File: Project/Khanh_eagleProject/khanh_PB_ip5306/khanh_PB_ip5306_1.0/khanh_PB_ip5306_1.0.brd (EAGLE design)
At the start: 27 x 16 mm, 18 parts

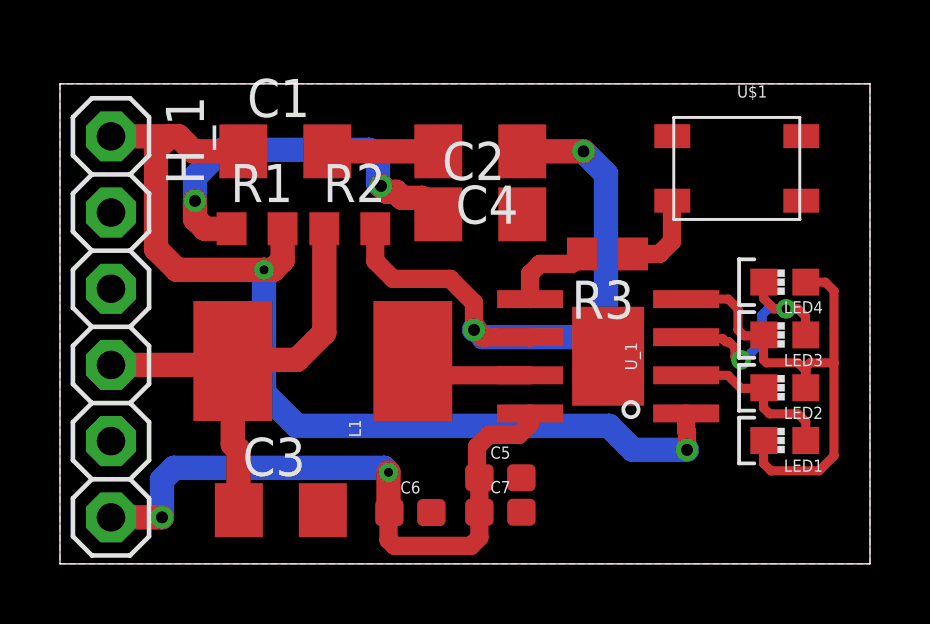
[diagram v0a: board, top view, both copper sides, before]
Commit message: chỉnh sửa pcd mạch sạc ip5306
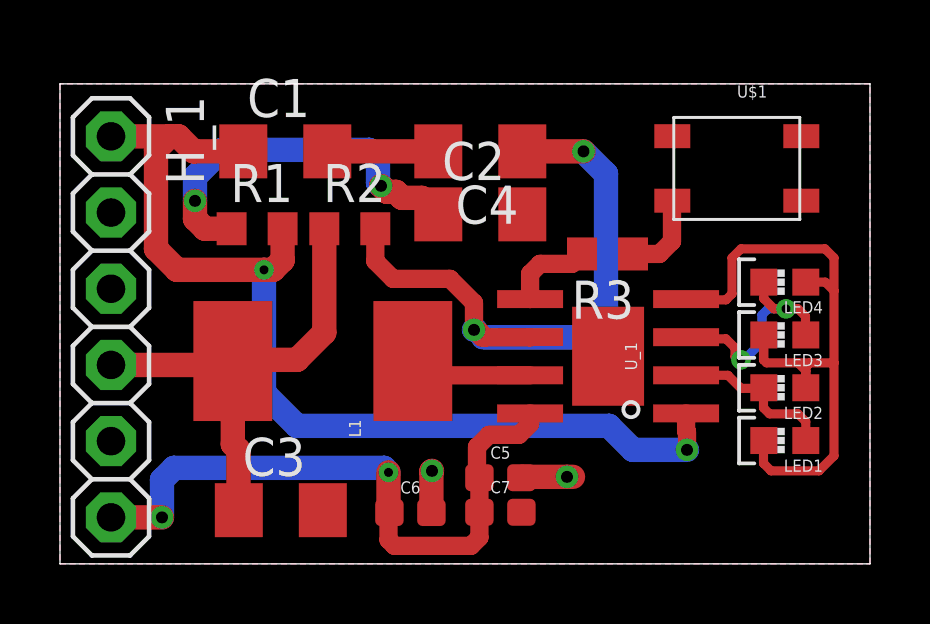
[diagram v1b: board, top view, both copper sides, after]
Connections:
- net VIN renamed S'HO
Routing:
- net N$7: track 18.2 -> 23.4 mm
- net GND: track 3.70 -> 6.83 mm, vias 0 -> 2
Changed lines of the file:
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@@
 <grid distance="0.1" unitdist="mm" unit="mm" style="lines" multiple="1" display="yes" altdistance="0.05" altunitdist="mm" altunit="mm"/>
 <layers>
-<layer number="1" name="Top" color="4" fill="1" visible="no" active="yes"/>
+<layer number="1" name="Top" color="4" fill="1" visible="yes" active="yes"/>
 <layer number="2" name="Route2" color="1" fill="3" visible="no" active="no"/>
 <layer number="3" name="Route3" color="4" fill="3" visible="no" active="no"/>
@@
 <layer number="21" name="tPlace" color="7" fill="1" visible="no" active="yes"/>
 <layer number="22" name="bPlace" color="7" fill="1" visible="no" active="yes"/>
-<layer number="23" name="tOrigins" color="15" fill="1" visible="no" active="yes"/>
+<layer number="23" name="tOrigins" color="15" fill="1" visible="yes" active="yes"/>
 <layer number="24" name="bOrigins" color="15" fill="1" visible="yes" active="yes"/>
 <layer number="25" name="tNames" color="7" fill="1" visible="no" active="yes"/>
@@
 <layer number="27" name="tValues" color="7" fill="1" visible="no" active="yes"/>
 <layer number="28" name="bValues" color="7" fill="1" visible="no" active="yes"/>
-<layer number="29" name="tStop" color="7" fill="3" visible="no" active="yes"/>
+<layer number="29" name="tStop" color="7" fill="3" visible="yes" active="yes"/>
 <layer number="30" name="bStop" color="7" fill="6" visible="yes" active="yes"/>
 <layer number="31" name="tCream" color="7" fill="4" visible="no" active="yes"/>
@@
 </elements>
 <signals>
-<signal name="VIN">
+<signal name="S'HO">
 <contactref element="U_1" pad="1"/>
 <contactref element="R1" pad="2"/>
@@
 </polygon>
 <wire x1="8.91" y1="13.75" x2="12.61" y2="13.75" width="0.8128" layer="1"/>
-<wire x1="12.38" y1="1.71" x2="15.38" y2="1.72" width="0" layer="19" extent="1-1"/>
-<wire x1="1.7" y1="9.17" x2="1.7" y2="4.09" width="0" layer="19" extent="1-1"/>
 <polygon width="0.254" layer="16" isolate="0.3048" rank="6">
 <vertex x="0" y="0"/>
@@
 <vertex x="0" y="16"/>
 </polygon>
+<wire x1="12.38" y1="1.71" x2="12.38" y2="3.08" width="0.8128" layer="1"/>
+<wire x1="12.38" y1="3.08" x2="12.4" y2="3.1" width="0.8128" layer="1"/>
+<wire x1="17.1" y1="2.9" x2="16.9" y2="2.9" width="0.8128" layer="1"/>
+<wire x1="16.9" y1="2.9" x2="15.41" y2="2.9" width="0.8128" layer="1"/>
+<wire x1="15.41" y1="2.9" x2="15.38" y2="2.87" width="0.8128" layer="1"/>
+<via x="12.4" y="3.1" extent="1-16" drill="0.4" diameter="0.7"/>
+<via x="16.9" y="2.9" extent="1-16" drill="0.4" diameter="0.7"/>
 </signal>
 <signal name="N$1">
@@
 <wire x1="24.86" y1="6.44" x2="24.6" y2="6.7" width="0.3048" layer="1"/>
 <wire x1="24.6" y1="6.7" x2="23.55" y2="6.7" width="0.3048" layer="1"/>
-<wire x1="23.55" y1="6.7" x2="23.45" y2="6.8" width="0.3048" layer="1"/>
 <wire x1="23.45" y1="6.8" x2="23.45" y2="7.62" width="0.3048" layer="1"/>
 <wire x1="23.45" y1="7.62" x2="23.46" y2="7.63" width="0.3048" layer="1"/>
@@
 <wire x1="23.45" y1="3.35" x2="23.45" y2="4.1" width="0.3048" layer="1"/>
 <wire x1="23.45" y1="4.1" x2="23.46" y2="4.11" width="0.3048" layer="1"/>
-<wire x1="20.87" y1="8.825" x2="22.275" y2="8.825" width="0.3048" layer="1"/>
-<wire x1="22.275" y1="8.825" x2="22.6" y2="8.5" width="0.3048" layer="1"/>
-<wire x1="22.6" y1="8.5" x2="22.6" y2="7.8" width="0.3048" layer="1"/>
-<wire x1="22.6" y1="7.8" x2="22.8" y2="7.6" width="0.3048" layer="1"/>
-<wire x1="22.8" y1="7.6" x2="23.43" y2="7.6" width="0.3048" layer="1"/>
-<wire x1="23.43" y1="7.6" x2="23.46" y2="7.63" width="0.3048" layer="1"/>
 <wire x1="24.86" y1="5.87" x2="24.86" y2="6.56" width="0.3048" layer="1"/>
 <wire x1="24.86" y1="6.56" x2="25" y2="6.7" width="0.3048" layer="1"/>
 <wire x1="25" y1="6.7" x2="25.8" y2="6.7" width="0.3048" layer="1"/>
+<wire x1="23.46" y1="7.63" x2="23.46" y2="6.81" width="0.3048" layer="1"/>
+<wire x1="23.46" y1="6.81" x2="23.45" y2="6.8" width="0.3048" layer="1"/>
+<wire x1="23.45" y1="6.8" x2="23.55" y2="6.7" width="0.3048" layer="1"/>
+<wire x1="24.6" y1="6.7" x2="25" y2="6.7" width="0.3048" layer="1"/>
+<wire x1="25.8" y1="9.1" x2="25.8" y2="10.2" width="0.3048" layer="1"/>
+<wire x1="25.8" y1="10.2" x2="25.5" y2="10.5" width="0.3048" layer="1"/>
+<wire x1="25.5" y1="10.5" x2="22.7" y2="10.5" width="0.3048" layer="1"/>
+<wire x1="22.7" y1="10.5" x2="22.4" y2="10.2" width="0.3048" layer="1"/>
+<wire x1="22.4" y1="10.2" x2="22.4" y2="9" width="0.3048" layer="1"/>
+<wire x1="22.4" y1="9" x2="22.2" y2="8.8" width="0.3048" layer="1"/>
+<wire x1="22.2" y1="8.8" x2="20.895" y2="8.8" width="0.3048" layer="1"/>
+<wire x1="20.895" y1="8.8" x2="20.87" y2="8.825" width="0.3048" layer="1"/>
 </signal>
 <signal name="N$8">
@@
 <wire x1="22.6" y1="6.8" x2="22.5" y2="6.9" width="0.3048" layer="1"/>
 <wire x1="22.5" y1="6.9" x2="22.5" y2="7.2" width="0.3048" layer="1"/>
-<wire x1="22.5" y1="7.2" x2="22.3" y2="7.4" width="0.3048" layer="1"/>
-<wire x1="22.3" y1="7.4" x2="22.2" y2="7.4" width="0.3048" layer="1"/>
-<wire x1="22.2" y1="7.4" x2="22.1" y2="7.5" width="0.3048" layer="1"/>
-<wire x1="22.1" y1="7.5" x2="20.925" y2="7.5" width="0.3048" layer="1"/>
+<wire x1="22.5" y1="7.2" x2="22.2" y2="7.5" width="0.3048" layer="1"/>
+<wire x1="22.2" y1="7.5" x2="20.925" y2="7.5" width="0.3048" layer="1"/>
 <wire x1="20.925" y1="7.5" x2="20.87" y2="7.555" width="0.3048" layer="1"/>
 </signal>
